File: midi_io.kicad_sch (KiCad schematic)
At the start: 0 parts

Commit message: Added oled hierarchical page and referenced other pages
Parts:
- added C?: 100n, Capacitor_SMD:C_0603_1608Metric, symbol Device:C_Small
- added D?: 1N4148WS, Diode_SMD:D_SOD-323, symbol Diode:1N4148WS
- added J?: Midi In Jack, Connector_Audio:Jack_3.5mm_CUI_SJ1-3513N_Horizontal, symbol ksoloti_shield_symbols:AudioJack3_3.5mm_Stereo_SwitchT_WQP729JH-Blue_from_Thonk
- added J?: Midi Out Jack, Connector_Audio:Jack_3.5mm_CUI_SJ1-3513N_Horizontal, symbol ksoloti_shield_symbols:AudioJack3_3.5mm_Stereo_SwitchT_WQP729JH-Blue_from_Thonk
- added OK?: 6N137, Package_DIP:SMDIP-8_W9.53mm, symbol Isolator:6N137
- added R?: 220, Resistor_SMD:R_0603_1608Metric, symbol Device:R
- added R?: 10k, Resistor_SMD:R_0603_1608Metric, symbol Device:R
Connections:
- new net: J?.R, R?.1
- new net: D?.2 (A), J?.T, OK?.3 (C)
- new net: D?.1 (K), OK?.2 (A), R?.2
- new net +5V: C?.1, OK?.8 (VCC), R?.2
- new net GND: C?.2, J?.S, OK?.5 (GND)
- new net MIDI_RX: OK?.6 (VO), R?.1
- new net MO4: J?.R
- new net MO5: J?.T
- no-connect marks 0 -> 4
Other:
- note added: "MIDI In"
- note added: "MIDI Out"

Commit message: Annotated all components (numerating)
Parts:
- gave numbers to parts that had none: 7
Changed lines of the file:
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@@
 		(dnp no)
 		(fields_autoplaced yes)
-		(property "Reference" "J?"
+		(property "Reference" "J_MIDI_IN1"
 			(at 51.435 41.91 0)
 			(effects
@@
 			(project "diggi_shield_2"
 				(path "/21684161-6457-4723-8fc3-25d7330779e2/4a23c275-8685-4316-ac30-e93166529349"
-					(reference "J?")
+					(reference "J_MIDI_IN1")
 					(unit 1)
 				)
@@
 		(dnp no)
 		(fields_autoplaced yes)
-		(property "Reference" "OK?"
+		(property "Reference" "OK1"
 			(at 86.36 36.83 0)
 			(effects
@@
 			(project "diggi_shield_2"
 				(path "/21684161-6457-4723-8fc3-25d7330779e2/4a23c275-8685-4316-ac30-e93166529349"
-					(reference "OK?")
+					(reference "OK1")
 					(unit 1)
 				)
@@
 		(on_board yes)
 		(dnp no)
-		(property "Reference" "R?"
+		(property "Reference" "R32"
 			(at 69.0153 46.482 0)
 			(effects
@@
 			(project "diggi_shield_2"
 				(path "/21684161-6457-4723-8fc3-25d7330779e2/4a23c275-8685-4316-ac30-e93166529349"
-					(reference "R?")
+					(reference "R32")
 					(unit 1)
 				)
@@
 		(dnp no)
 		(fields_autoplaced yes)
-		(property "Reference" "D?"
+		(property "Reference" "D3"
 			(at 76.2 50.7999 90)
 			(effects
@@
 			(project "diggi_shield_2"
 				(path "/21684161-6457-4723-8fc3-25d7330779e2/4a23c275-8685-4316-ac30-e93166529349"
-					(reference "D?")
+					(reference "D3")
 					(unit 1)
 				)
@@
 		(on_board yes)
 		(dnp no)
-		(property "Reference" "C?"
+		(property "Reference" "C28"
 			(at 100.1268 35.6616 0)
 			(effects
@@
 			(project "diggi_shield_2"
 				(path "/21684161-6457-4723-8fc3-25d7330779e2/4a23c275-8685-4316-ac30-e93166529349"
-					(reference "C?")
+					(reference "C28")
 					(unit 1)
 				)
@@
 		(dnp no)
 		(fields_autoplaced yes)
-		(property "Reference" "J?"
+		(property "Reference" "J_MIDI_OUT1"
 			(at 51.435 83.82 0)
 			(effects
@@
 			(project "diggi_shield_2"
 				(path "/21684161-6457-4723-8fc3-25d7330779e2/4a23c275-8685-4316-ac30-e93166529349"
-					(reference "J?")
+					(reference "J_MIDI_OUT1")
 					(unit 1)
 				)
@@
 		(on_board yes)
 		(dnp no)
-		(property "Reference" "R?"
+		(property "Reference" "R33"
 			(at 103.632 46.5547 0)
 			(effects
@@
 			(project "diggi_shield_2"
 				(path "/21684161-6457-4723-8fc3-25d7330779e2/4a23c275-8685-4316-ac30-e93166529349"
-					(reference "R?")
-					(unit 1)
-				)
+					(reference "R33")
+					(unit 1)
+				)

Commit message: Cleaned up ERC errors
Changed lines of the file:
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@@
 	(wire
 		(pts
-			(xy 97.79 64.77) (xy 105.41 64.77)
+			(xy 109.22 49.53) (xy 105.41 49.53)
 		)
 		(stroke
@@
 		(pts
 			(xy 73.66 55.88) (xy 78.74 55.88)
-		)
-		(stroke
-			(width 0)
-			(type default)
-		)
-	)
-	(wire
-		(pts
-			(xy 105.41 64.77) (xy 105.41 49.53)
 		)
 		(stroke
@@
 	(global_label "MIDI_RX"
 		(shape input)
-		(at 97.79 64.77 180)
+		(at 109.22 49.53 0)
 		(fields_autoplaced yes)
 		(effects
@@
 				(size 1.27 1.27)
 			)
-			(justify right)
+			(justify left)
 		)
 		(property "Intersheetrefs" "${INTERSHEET_REFS}"
-			(at 87.9988 64.6906 0)
+			(at 119.0112 49.4506 0)
 			(effects
 				(font
 					(size 1.27 1.27)
 				)
-				(justify right)
+				(justify left)
 				(hide yes)
 			)

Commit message: Solve all warnings
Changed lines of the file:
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@@
-		(color 0 0 0 0)
-	)
-	(junction
-		(at 58.42 87.63)
-		(diameter 0)
-		(color 0 0 0 0)
-	)
-	(junction
-		(at 58.42 95.25)
-		(diameter 0)
-		(color 0 0 0 0)
-	)
-	(junction
-		(at 58.42 90.17)
-		(diameter 0)
 		(color 0 0 0 0)
 	)
@@
 		(pts
 			(xy 58.42 55.88) (xy 73.66 55.88)
-		)
-		(stroke
-			(width 0)
-			(type default)
-		)
-	)
-	(wire
-		(pts
-			(xy 57.15 95.25) (xy 58.42 95.25)
 		)
 		(stroke
@@
 	(wire
 		(pts
-			(xy 58.42 90.17) (xy 68.58 90.17)
-		)
-		(stroke
-			(width 0)
-			(type default)
-		)
-	)
-	(wire
-		(pts
 			(xy 58.42 50.8) (xy 64.77 50.8)
 		)
@@
 	(wire
 		(pts
-			(xy 57.15 87.63) (xy 58.42 87.63)
+			(xy 105.41 49.53) (xy 93.98 49.53)
 		)
 		(stroke
@@
 	(wire
 		(pts
-			(xy 105.41 49.53) (xy 93.98 49.53)
+			(xy 58.42 85.09) (xy 58.42 87.63)
 		)
 		(stroke
@@
 	(wire
 		(pts
-			(xy 64.77 50.8) (xy 64.77 48.26)
+			(xy 58.42 90.17) (xy 68.58 90.17)
 		)
 		(stroke
@@
 	(wire
 		(pts
-			(xy 58.42 85.09) (xy 58.42 87.63)
+			(xy 64.77 50.8) (xy 64.77 48.26)
 		)
 		(stroke
@@
 		)
 		(stroke
-			(width 0)
-			(type default)
-		)
-	)
-	(wire
-		(pts
-			(xy 55.88 90.17) (xy 58.42 90.17)
-		)
-		(stroke

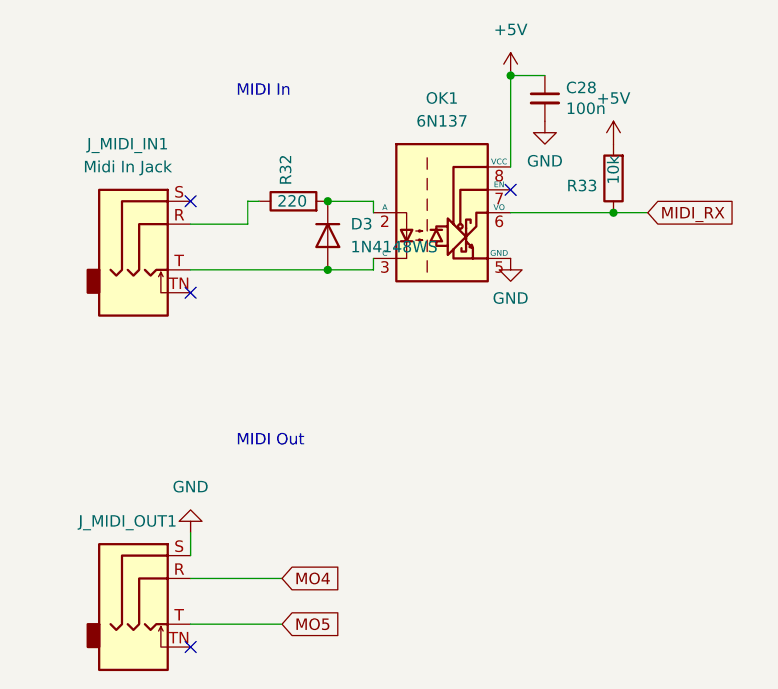
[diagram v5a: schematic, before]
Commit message: Remove symbol copy warnings
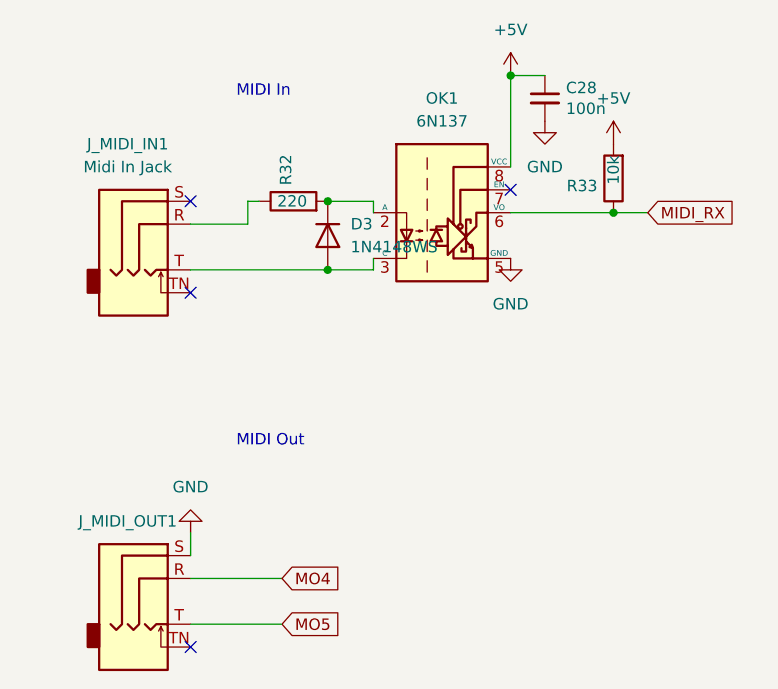
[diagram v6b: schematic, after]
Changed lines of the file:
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@@
 			)
 		)
-		(property "Description" ""
+		(property "Description" "Power symbol creates a global label with name \"+5V\""
 			(at 93.98 34.29 0)
 			(effects
@@
 		)
 		(property "Value" "GND"
-			(at 93.98 59.0534 0)
+			(at 93.98 59.69 0)
 			(effects
 				(font
@@
 			)
 		)
-		(property "Description" ""
+		(property "Description" "Power symbol creates a global label with name \"GND\" , ground"
 			(at 93.98 54.61 0)
 			(effects
@@
 			)
 		)
-		(property "Description" ""
+		(property "Description" "Power symbol creates a global label with name \"+5V\""
 			(at 105.41 41.91 0)
 			(effects
@@
 		)
 		(property "Value" "GND"
-			(at 97.79 43.8134 0)
+			(at 97.79 44.45 0)
 			(effects
 				(font
@@
 			)
 		)
-		(property "Description" ""
+		(property "Description" "Power symbol creates a global label with name \"GND\" , ground"
 			(at 97.79 39.37 0)
 			(effects
@@
 			)
 		)
-		(property "Description" ""
+		(property "Description" "Power symbol creates a global label with name \"GND\" , ground"
 			(at 58.42 85.09 0)
 			(effects

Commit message: Removed final warnings
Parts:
- OK1: symbol Isolator:6N137 -> diggi:6N137_Diggi
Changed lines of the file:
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@@
 	)
 	(symbol
-		(lib_id "Isolator:6N137")
+		(lib_id "diggi:6N137_Diggi")
 		(at 86.36 49.53 0)
 		(unit 1)
@@
 			)
 		)
-		(property "Description" ""
+		(property "Description" "75V 0.15A Fast switching Diode, SOD-323"
 			(at 73.66 52.07 0)
 			(effects
+				(font
+					(size 1.27 1.27)
+				)
+				(hide yes)
+			)
+		)
+		(property "Sim.Device" "D"
+			(at 73.66 52.07 0)
+			(effects
+				(font
+					(size 1.27 1.27)
+				)
+				(hide yes)
+			)
+		)
+		(property "Sim.Pins" "1=K 2=A"
+			(at 73.66 52.07 0)
+			(effects

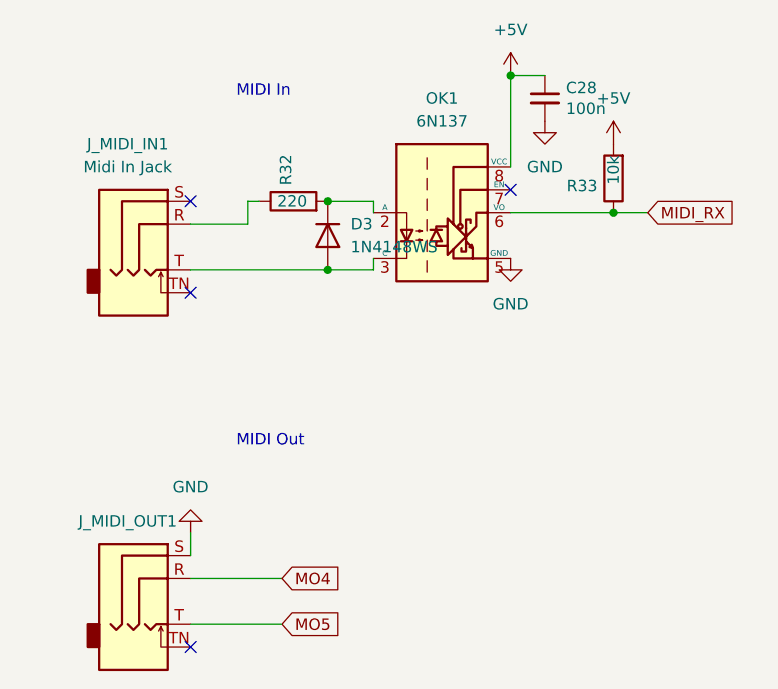
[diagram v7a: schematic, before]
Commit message: Added jack symbols and footprints also footprints for ics and caps
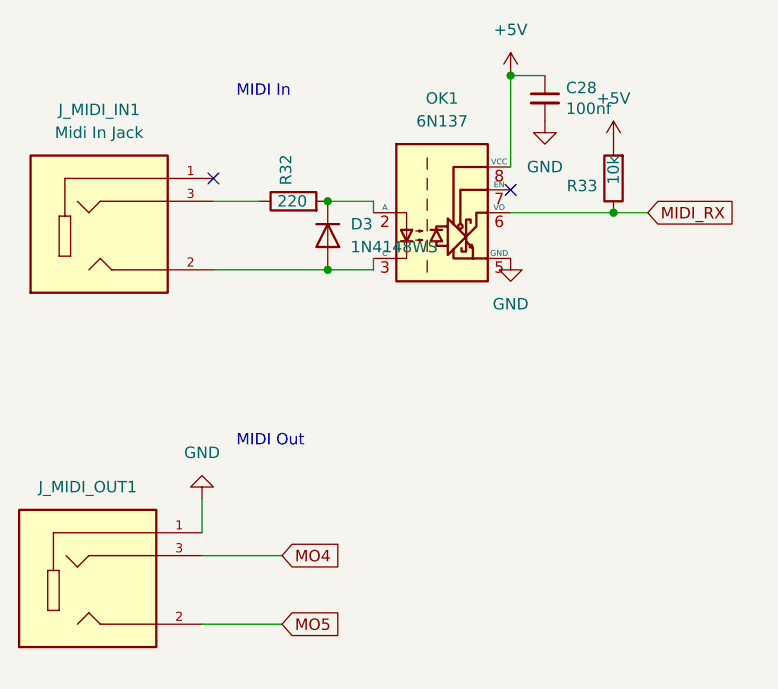
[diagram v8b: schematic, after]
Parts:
- C28: value 100n -> 100nf
- J_MIDI_IN1, J_MIDI_OUT1: footprint Connector_Audio:Jack_3.5mm_CUI_SJ1-3513N_Horizontal -> diggi_footprints:CUI_SJ1-3523N; symbol ksoloti_shield_symbols:AudioJack3_3.5mm_Stereo_SwitchT_WQP729JH-Blue_from_Thonk -> SJ1-3523N:SJ1-3523N; Availability (none) -> In Stock; Check_prices (none) -> https://www.snapeda.com/parts/SJ1-3523N/Same+Sky/view-part/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; Description_1 (none) -> 3.5 mm, Stereo, Right Angle, Through Hole, 3 Conductors, 0 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; MANUFACTURER (none) -> CUI Devices; MAXIMUM_PACKAGE_HEIGHT (none) -> 6.25 mm; MF (none) -> Same Sky; MP (none) -> SJ1-3523N; PARTREV (none) -> 1.05; Package (none) -> None; Price (none) -> None; Purchase-URL (none) -> https://www.snapeda.com/api/url_track_click_mouser/?unipart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; STANDARD (none) -> Manufacturer Recommendations; SnapEDA_Link (none) -> https://www.snapeda.com/parts/SJ1-3523N/Same+Sky/view-part/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
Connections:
- net GND: now also J_MIDI_OUT1.1; no longer J_MIDI_OUT1.S
- net MO4: now also J_MIDI_OUT1.3; no longer J_MIDI_OUT1.R
- net MO5: now also J_MIDI_OUT1.2; no longer J_MIDI_OUT1.T
- net at R32.1: now also J_MIDI_IN1.3; no longer J_MIDI_IN1.R
- net at D3.2 (A), OK1.3 (C): now also J_MIDI_IN1.2; no longer J_MIDI_IN1.T
- no-connect marks 4 -> 2
